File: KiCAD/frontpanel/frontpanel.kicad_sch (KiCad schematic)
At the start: 23 parts, among them J1 8P8C_Shielded, Q1 2N7000, Q2 2N7000, Q3 2N7000, U1 Adafruit_PCF8575_Breakout

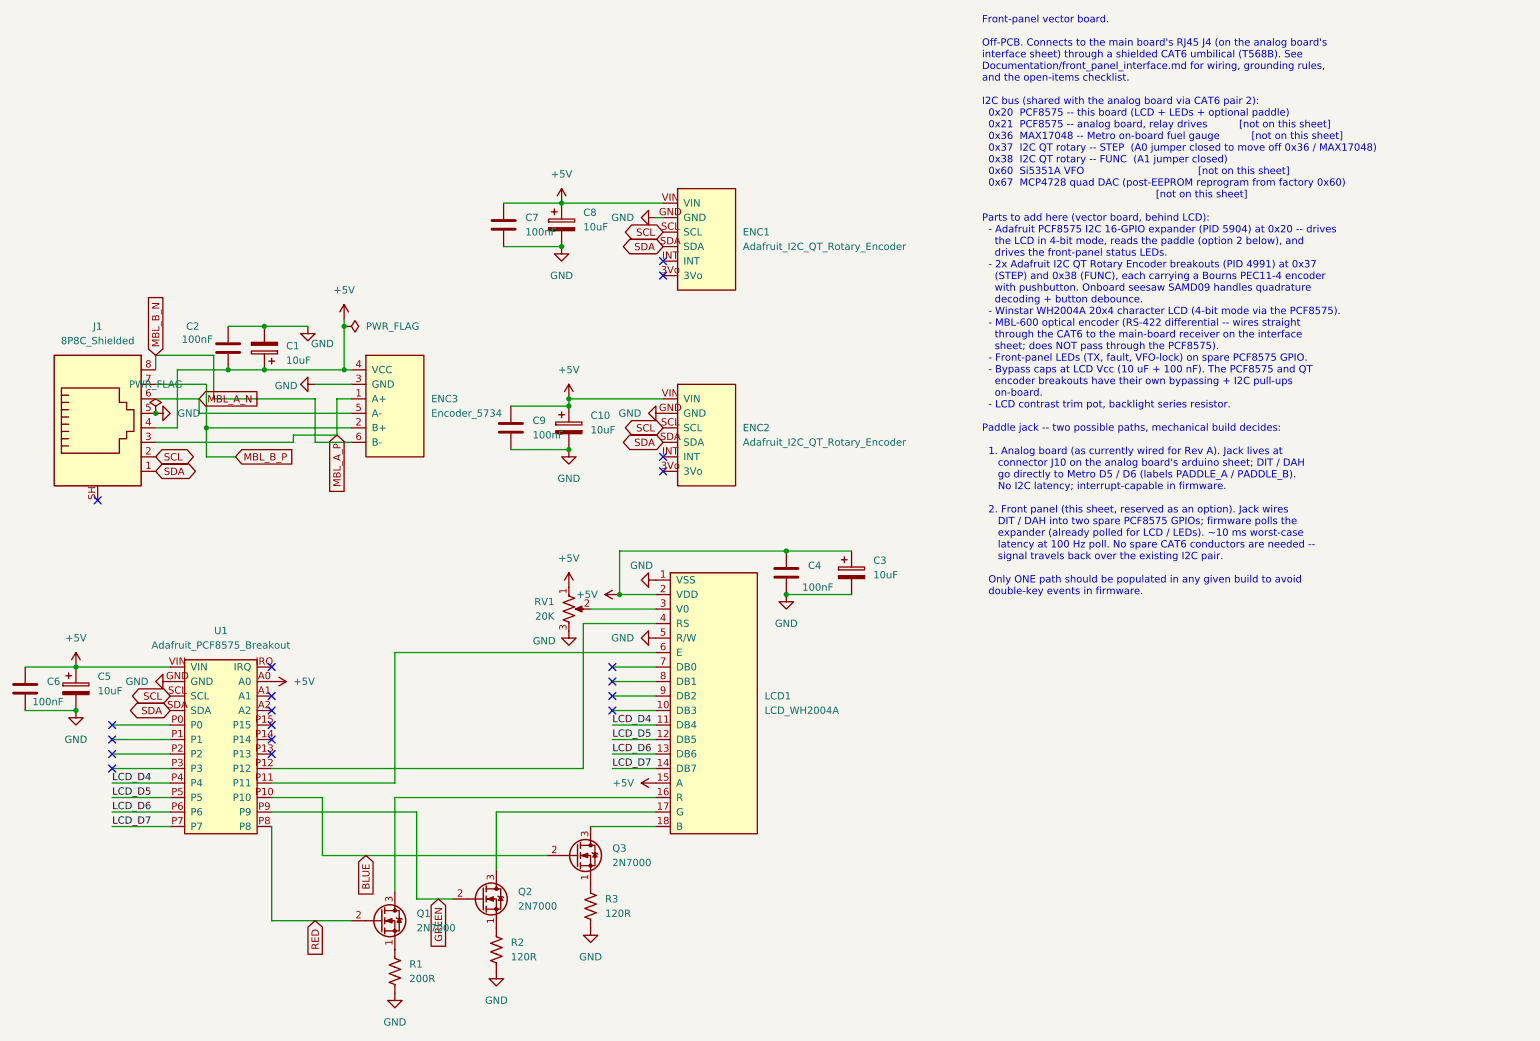
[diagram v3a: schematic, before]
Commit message: Front-panel: PCF8575 address fix, MCP4725 for LCD contrast, footprints, i2c_bus.md
PCF8575 A0/A1 configuration had the two boards' addresses swapped in
all documentation, firmware, and the frontpanel schematic text note.
Actual wiring: main-board U17 (arduino sheet, A0 open) = 0x20 for relay
drives; front-panel U1 (A0 jumper closed) = 0x21 for LCD/LEDs. Fixed
in firmware/main/pin_map.h, front_panel_interface.md, and (user-side)
the schematic text note.

Assign footprints to all previously-unassigned components on the
front-panel schematic, using the analog board's conventions:
  - Device:C 100nF          -> Capacitor_THT:C_Disc_D5.0mm_W2.5mm_P5.00mm
  - Device:C_Polarized 10uF -> Capacitor_THT:CP_Radial_D5.0mm_P2.00mm
  - Device:R_US 120R/200R   -> Resistor_THT:R_Axial_DIN0207_...
  - Device:R_Potentiometer_US -> Potentiometer_THT:Bourns_3296W_Vertical

Add MCP4725 for software-controlled LCD contrast:
  - New xmitter:MCP4725 symbol, style matching MCP4728.
  - New xmitter:Adafruit_MCP4725_Breakout footprint. Dimensions
    verified from Adafruit fab print (not datasheet text -- lesson
    from the RJE1D-188 draft error). Board 25.4 x 17.78 mm, mounting
    holes on 20.32 x 12.70 mm, 6-pin THT header VIN/GND/SCL/SDA/A0/VOUT.
  - MCP4725 lives at 0x62 (A0 open). VOUT drives LCD V0 directly,
    allowing firmware-controlled contrast in place of the RV1 pot.

Add Documentation/i2c_bus.md as the single source of truth for I2C
device addresses across all three PCBs. Referenced from CLAUDE.md's
design-reference table. When an address changes, update this file
first; other docs, firmware pin_map.h, and schematic text notes mirror.

frontpanel.kicad_pcb: initial layout file created (empty board layout
started, populated with symbols from the schematic).

Co-Authored-By: Claude Opus 4.7 <noreply@anthropic.com>
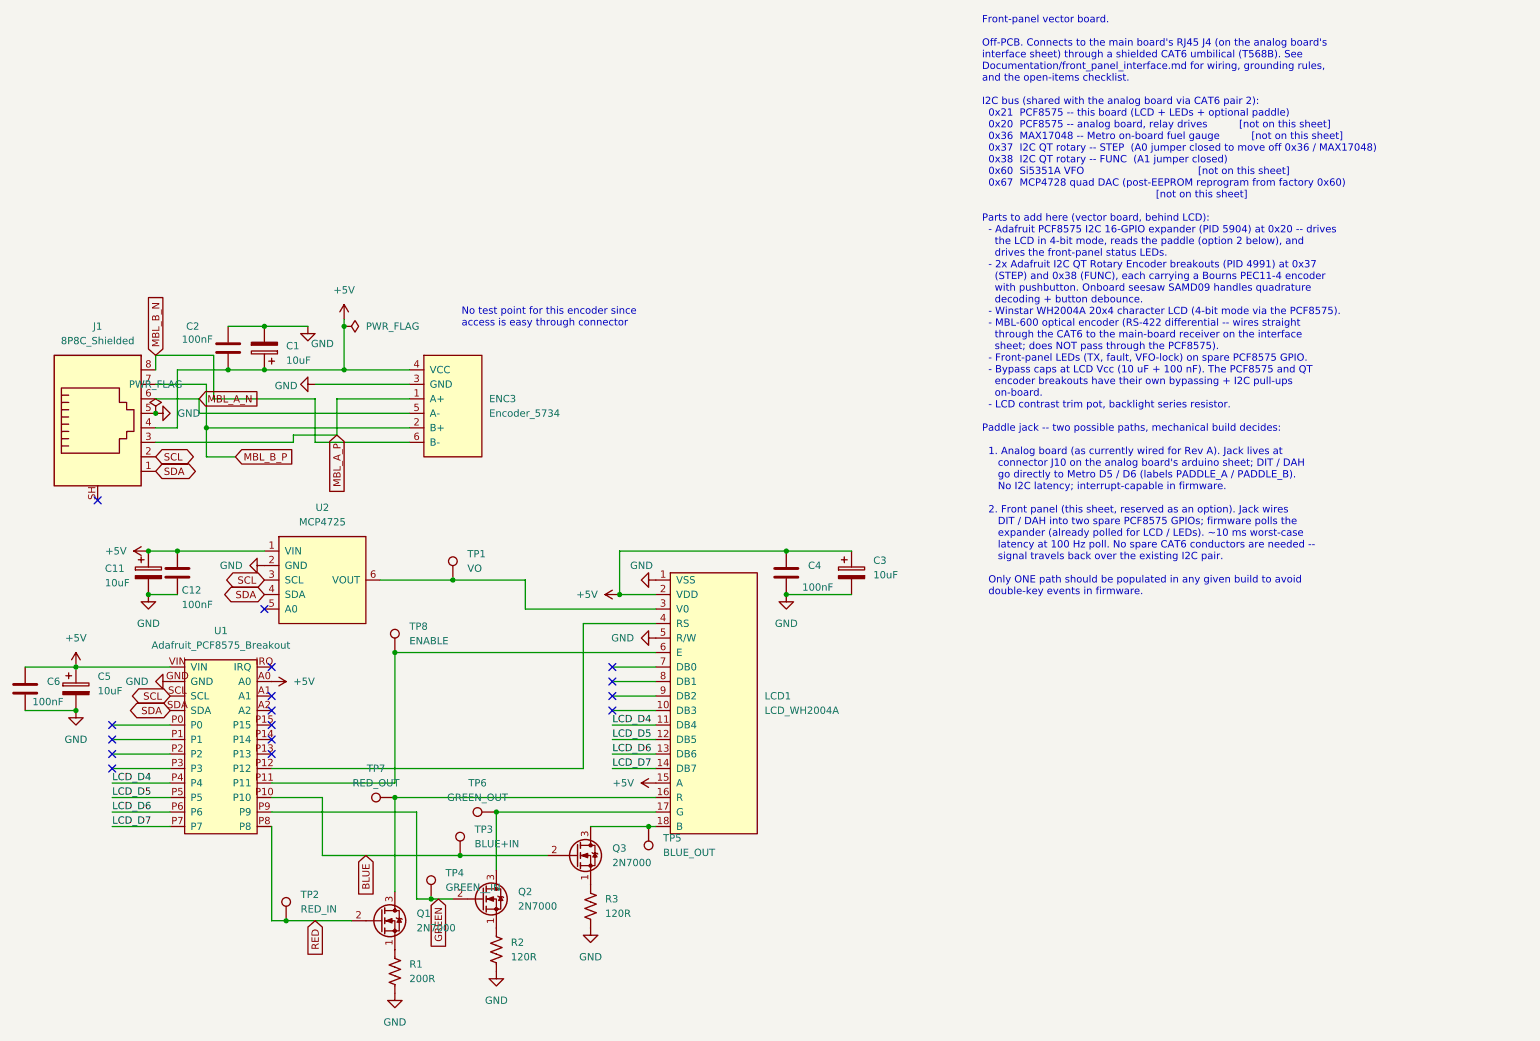
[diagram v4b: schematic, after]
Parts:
- removed C10, C8: 10uF, symbol Device:C_Polarized
- removed C7, C9: 100nF, symbol Device:C
- removed ENC1, ENC2: Adafruit_I2C_QT_Rotary_Encoder, xmitter:Adafruit_I2C_QT_Rotary_Encoder, symbol xmitter:Adafruit_I2C_QT_Rotary_Encoder
- removed RV1: 20K, symbol Device:R_Potentiometer_US
- added C11: 10uF, Capacitor_THT:CP_Radial_D5.0mm_P2.00mm, symbol Device:C_Polarized
- added C12: 100nF, Capacitor_THT:C_Disc_D5.0mm_W2.5mm_P5.00mm, symbol Device:C
- added TP1: VO, Connector_PinHeader_2.54mm:PinHeader_1x01_P2.54mm_Vertical, symbol xmitter:xTP
- added TP2: RED_IN, Connector_PinHeader_2.54mm:PinHeader_1x01_P2.54mm_Vertical, symbol xmitter:xTP
- added TP3: BLUE+IN, Connector_PinHeader_2.54mm:PinHeader_1x01_P2.54mm_Vertical, symbol xmitter:xTP
- added TP4: GREEN__IN, Connector_PinHeader_2.54mm:PinHeader_1x01_P2.54mm_Vertical, symbol xmitter:xTP
- added TP5: BLUE_OUT, Connector_PinHeader_2.54mm:PinHeader_1x01_P2.54mm_Vertical, symbol xmitter:xTP
- added TP6: GREEN_OUT, Connector_PinHeader_2.54mm:PinHeader_1x01_P2.54mm_Vertical, symbol xmitter:xTP
- added TP7: RED_OUT, Connector_PinHeader_2.54mm:PinHeader_1x01_P2.54mm_Vertical, symbol xmitter:xTP
- added TP8: ENABLE, Connector_PinHeader_2.54mm:PinHeader_1x01_P2.54mm_Vertical, symbol xmitter:xTP
- added U2: MCP4725, xmitter:Adafruit_MCP4725_Breakout, symbol xmitter:MCP4725
- C1, C3, C5: footprint (none) -> Capacitor_THT:CP_Radial_D5.0mm_P2.00mm
- C2, C4, C6: footprint (none) -> Capacitor_THT:C_Disc_D5.0mm_W2.5mm_P5.00mm
- R1, R2, R3: footprint (none) -> Resistor_THT:R_Axial_DIN0207_L6.3mm_D2.5mm_P10.16mm_Horizontal
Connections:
- net +5V: now also C11.1, C12.1, U2.1 (VIN)
- net BLUE: now also TP3.1
- net GND: now also C11.2, C12.2, U2.2 (GND)
- net GREEN: now also TP4.1
- net RED: now also TP2.1
- net SCL: now also U2.3 (SCL)
- net SDA: now also U2.4 (SDA)
- net at LCD1.16 (R), Q1.3 (D): now also TP7.1
- net at LCD1.6 (E), U1.P11: now also TP8.1
- net at LCD1.17 (G), Q2.3 (D): now also TP6.1
- net at LCD1.18 (B), Q3.3 (D): now also TP5.1
- net at LCD1.3 (V0): now also TP1.1, U2.6 (VOUT)
- no-connect marks 19 -> 16
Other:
- note added: "Front-panel vector board. Off-PCB. Connects to the main board's RJ45 J4 (on the analog board's interface sheet) through a shielded CAT6 umbilical (T568B). See Documentation/front_panel_interface.md for wiring, grounding rules, and the open-items checklist. I2C bus (shared with the analog board via CAT6 pair 2): 0x21 PCF8575 -- this board (LCD + LEDs + optional paddle) 0x20 PCF8575 -- analog board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"
- note added: "No test point for this encoder since access is easy through connector"
- note removed: "Front-panel vector board. Off-PCB. Connects to the main board's RJ45 J4 (on the analog board's interface sheet) through a shielded CAT6 umbilical (T568B). See Documentation/front_panel_interface.md for wiring, grounding rules, and the open-items checklist. I2C bus (shared with the analog board via CAT6 pair 2): 0x20 PCF8575 -- this board (LCD + LEDs + optional paddle) 0x21 PCF8575 -- analog board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"
- moved on the sheet: ENC3

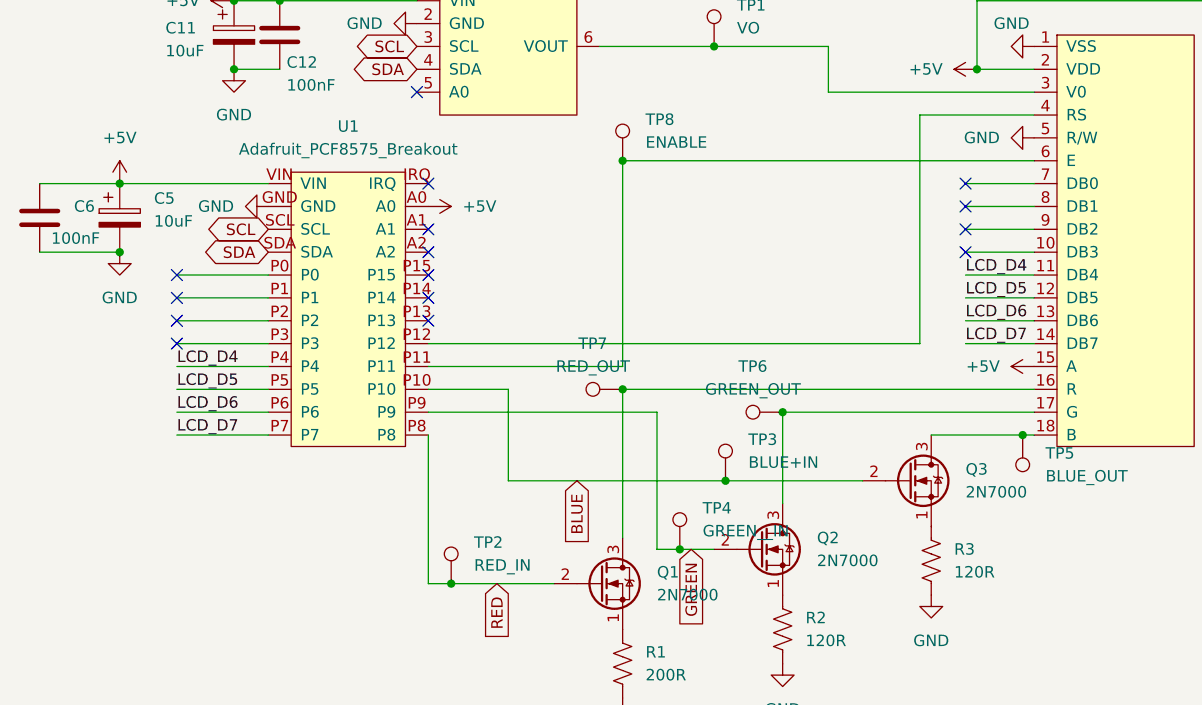
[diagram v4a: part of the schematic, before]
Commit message: Front-panel PCB: layout complete, DFM verified, ready for fab
Complete the front-panel PCB layout.  ERC clean, DRC clean except for
two silk_over_copper warnings on J1 SH pads (cosmetic; RJE1D-188
footprint silk box crosses the shield tab pads.  Irrelevant since the
shield is intentionally left floating on this board).

Layout details:

  - Board: 78 x 85 mm, 4x M3 corner mounting holes at 4 mm inset.
  - GND pours on F.Cu and B.Cu.  RJ45 shield isolation keepout
    (17.5 x 16 mm) on both layers prevents pour from touching the
    floating SH tabs.
  - Track widths 0.2 - 0.5 mm (JLC min 0.127 mm).  4 vias, 142 tracks.
  - Drill sizes 0.3 - 3.0 mm (JLC min 0.3 mm; aspect ratio 5.3:1 max
    on the 1.6 mm board).
  - J2 (Conn_01x03_Pin) added to bring out PCF8575 P13/P14/P15 for
    future use.  TP9 GND test point added.
  - PCF8575 P0-P3 also routed to LCD DB0-DB3: physically wired but
    ignored in 4-bit mode.  Per-pin jumpers at the LCD header let
    the trace be dropped if P0-P3 need reallocation.  8-bit mode
    is a firmware-only upgrade.
  - TP3 / TP4 value fields cleaned up (BLUE+IN -> BLUE_IN,
    GREEN__IN -> GREEN_IN).

Fix xmitter:Amphenol_RJE1D-188_Horizontal_Shielded footprint: previous
version had all Y coordinates negated relative to the PCB edge, which
caused the connector to sit backwards when placed.  Reworked to put
PCB edge below origin at Y=+8.8 and pin block above at Y=-3.96 /
Y=-6.50, matching the datasheet.

Docs:
  - front_panel_interface.md: full PCF8575 -> LCD pin allocation
    table, noting that P0-P3 are wired-but-ignored in 4-bit mode.
  - kicad_routing_cheatsheet.md: "B doesn't fill my pour"
    troubleshooting section (5 causes ordered by frequency).

Co-Authored-By: Claude Opus 4.7 <noreply@anthropic.com>
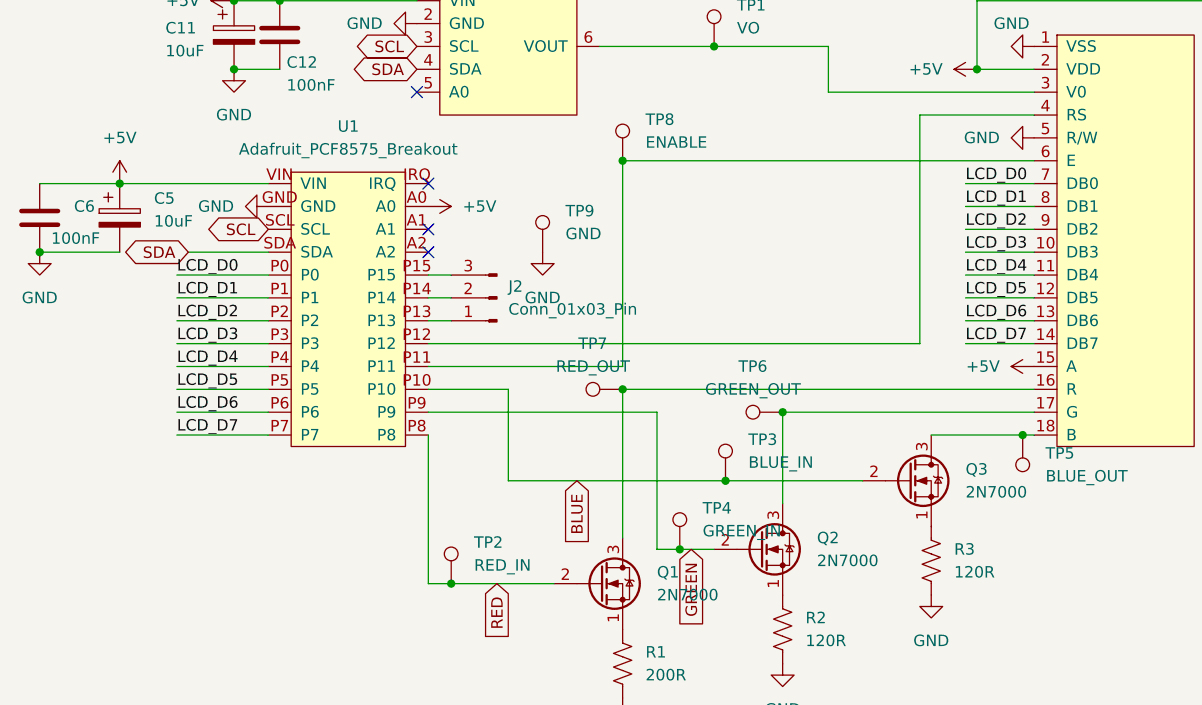
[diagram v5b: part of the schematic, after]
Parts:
- added J2: Conn_01x03_Pin, Connector_PinHeader_2.54mm:PinHeader_1x03_P2.54mm_Vertical, symbol Connector:Conn_01x03_Pin
- added TP9: GND, Connector_PinHeader_2.54mm:PinHeader_1x01_P2.54mm_Vertical, symbol xmitter:xTP
- TP3: value BLUE+IN -> BLUE_IN
- TP4: value GREEN__IN -> GREEN_IN
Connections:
- net GND: now also TP9.1
- net LCD_D0: now reaches U1.P0
- net LCD_D0: now also LCD1.7 (DB0)
- net LCD_D1: now reaches U1.P1
- net LCD_D1: now also LCD1.8 (DB1)
- net at U1.P13: now also J2.1 (Pin_1)
- net at U1.P14: now also J2.2 (Pin_2)
- net at U1.P15: now also J2.3 (Pin_3)
- net LCD_D2: now reaches U1.P2
- net LCD_D2: now also LCD1.9 (DB2)
- net LCD_D3: now reaches U1.P3
- net LCD_D3: now also LCD1.10 (DB3)
- no-connect marks 16 -> 5
